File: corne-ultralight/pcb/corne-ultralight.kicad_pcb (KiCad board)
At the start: 2 copper layers, 275.5 x 105.6 mm, 132 parts, among them J2 OLED, J5 Breakaway_Tabs, J7 OLED, SW1 SW_PUSH, SW10 SW_PUSH, SW11 SW_PUSH, SW12 SW_PUSH, SW13 SW_PUSH, SW14 SW_PUSH, SW15 SW_PUSH, SW16 SW_PUSH, SW17 SW_PUSH, SW18 SW_PUSH, SW19 SW_PUSH, SW2 SW_PUSH, SW20 SW_PUSH, SW21 SW_PUSH, SW22 SW_PUSH, SW23 SW_PUSH, SW24 SW_PUSH, SW25 SW_PUSH, SW26 SW_PUSH, SW27 SW_PUSH, SW28 SW_PUSH, SW29 SW_PUSH, SW3 SW_PUSH, SW30 SW_PUSH, SW31 SW_PUSH, SW32 SW_PUSH, SW33 SW_PUSH, SW34 SW_PUSH, SW35 SW_PUSH, SW36 SW_PUSH, SW37 SW_PUSH, SW38 SW_PUSH, SW39 SW_PUSH, SW4 SW_PUSH, SW40 SW_PUSH, SW41 SW_PUSH, SW42 SW_PUSH, SW5 SW_PUSH, SW6 SW_PUSH, SW7 SW_PUSH, SW8 SW_PUSH, SW9 SW_PUSH, U1 ProMicro, U2 ProMicro

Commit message: PCB updated with additional components
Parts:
- added BATJ3: Conn_01x02_Female, Connector_JST:JST_PH_S2B-PH-K_1x02_P2.00mm_Horizontal, F.Cu at (129.4, 95.7)
- added BATJ4: Conn_01x02_Female, Connector_JST:JST_PH_S2B-PH-K_1x02_P2.00mm_Horizontal, F.Cu at (137.3, 95.7)
- added BATJ7: Conn_01x02_Female, Connector_JST:JST_PH_S2B-PH-K_1x02_P2.00mm_Horizontal, F.Cu at (183.7, 89.0)
- added BATJ8: Conn_01x02_Female, Connector_JST:JST_PH_S2B-PH-K_1x02_P2.00mm_Horizontal, F.Cu at (191.6, 89.0)
- added OL1: OLED, kbd:OLED_1side, F.Cu at (128.1, 104.7)
- added OL2: OLED, kbd:OLED_1side, F.Cu at (168.1, 106.5)
- BATJ1: footprint Connector_PinHeader_2.54mm:PinHeader_1x02_P2.54mm_Vertical -> Connector_JST:JST_PH_S2B-PH-K_1x02_P2.00mm_Horizontal
- BATJ5: renamed from BATJ3; footprint Connector_PinHeader_2.54mm:PinHeader_1x02_P2.54mm_Vertical -> Connector_JST:JST_PH_S2B-PH-K_1x02_P2.00mm_Horizontal
- D1, D10, D11, D12, D13, D14, D15, D16, D17, D18, D19, D2, D20, D21, D22, D23, D24, D25, D26, D27, D28, D29, D3, D30, D31, D32, D33, D34, D35, D36, D37, D38, D39, D4, D40, D41, D42, D5, D6, D7, D8, D9: footprint kbd:D3_TH_SMD_v2 -> kbd:D3_TH
- renumbered BATJ4 to BATJ6

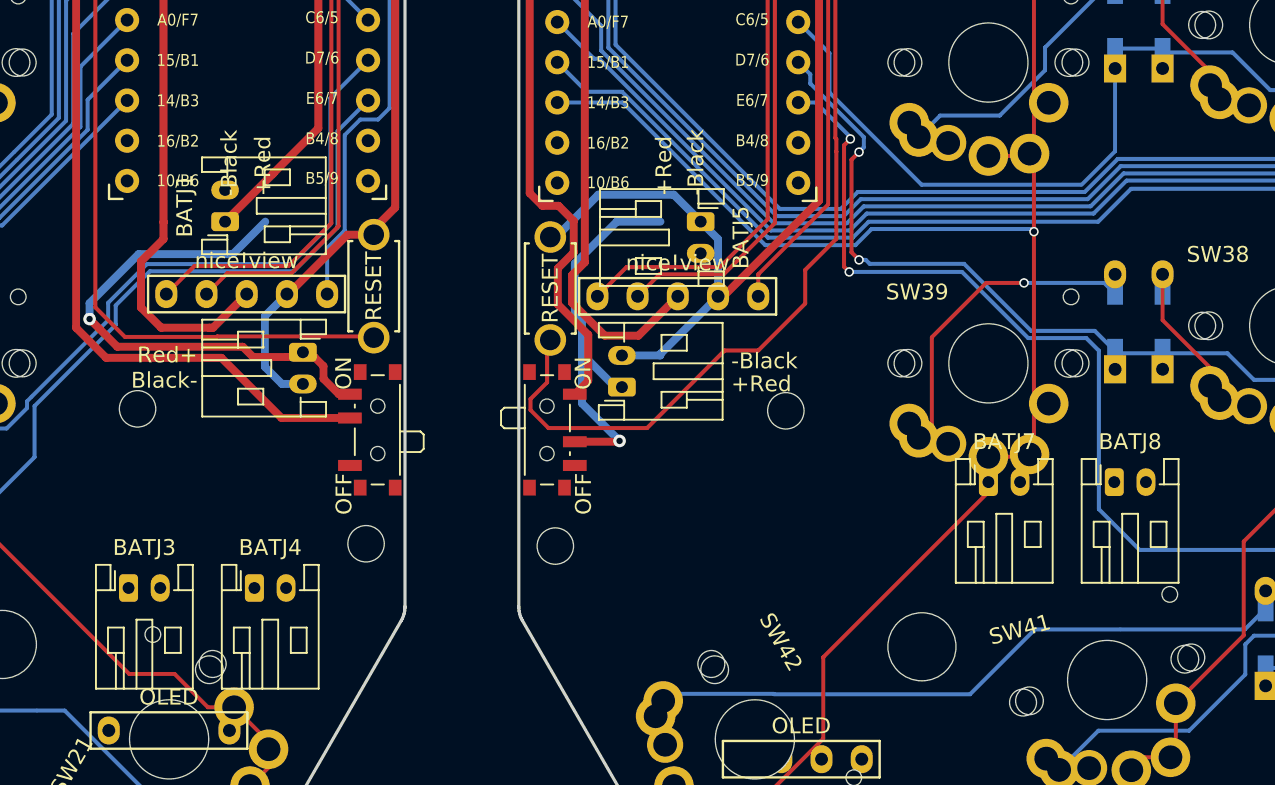
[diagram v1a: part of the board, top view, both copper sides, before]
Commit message: Bottom JST connectors aligned
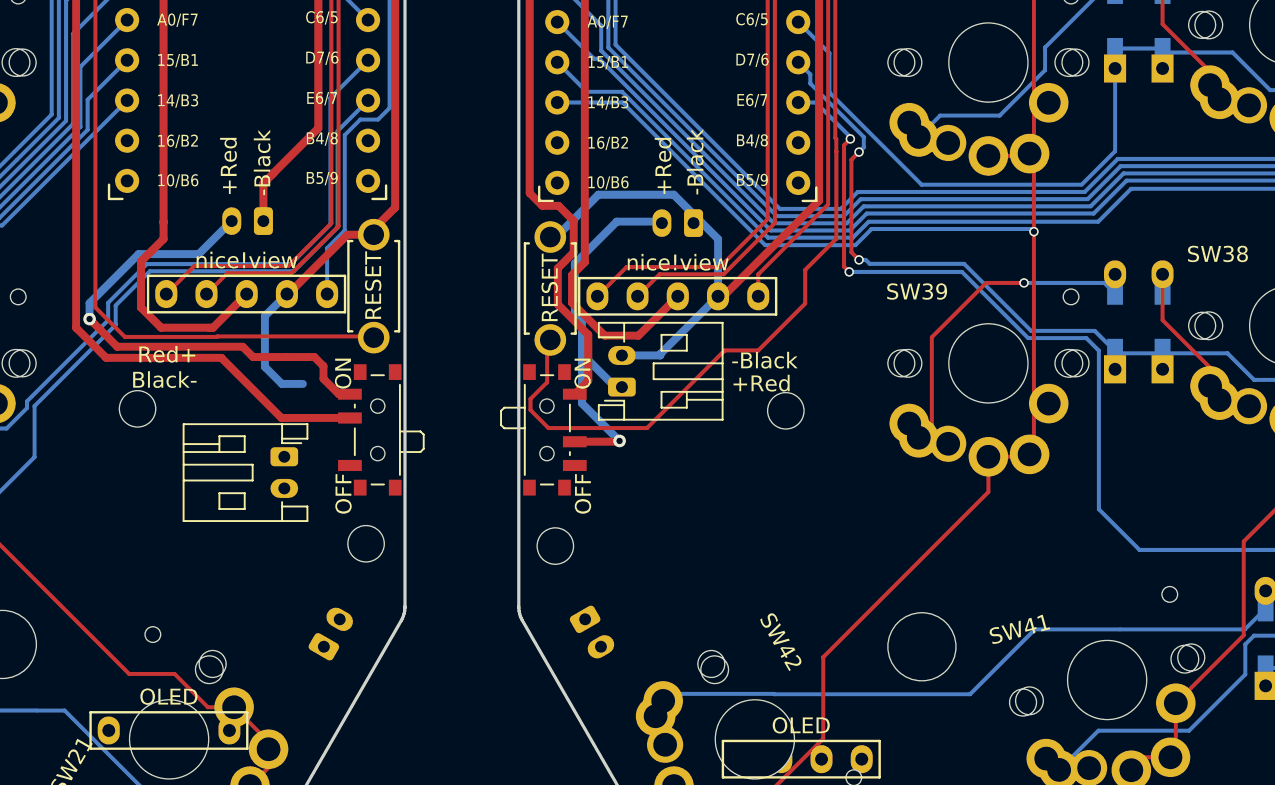
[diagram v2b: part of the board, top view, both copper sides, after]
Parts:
- removed the BATJ3 at (129.4, 95.7)
- removed BATJ8: Conn_01x02_Female, Connector_JST:JST_PH_S2B-PH-K_1x02_P2.00mm_Horizontal
- BATJ1: moved to B.Cu
- BATJ3: renamed from BATJ4; moved to B.Cu
- BATJ4: renamed from BATJ5; moved to B.Cu
- BATJ6: renamed from BATJ7; moved to B.Cu
- moved BATJ6 26.9 mm to (158.2, 97.7), turned to -60 degrees
- moved BATJ2 6.70 mm to (139.2, 87.4)
- moved BATJ3 5.75 mm to (141.7, 99.4), turned to 60 degrees
- moved BATJ1 2.42 mm to (137.9, 72.6), turned to 180 degrees
- moved BATJ4 0.46 mm to (165.1, 72.7), turned to 180 degrees
- renumbered BATJ6 to BATJ5
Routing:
- net Net-(BATJ1-Pin_2): track 33.1 -> 31.0 mm
- net GND: track 88.8 -> 87.7 mm

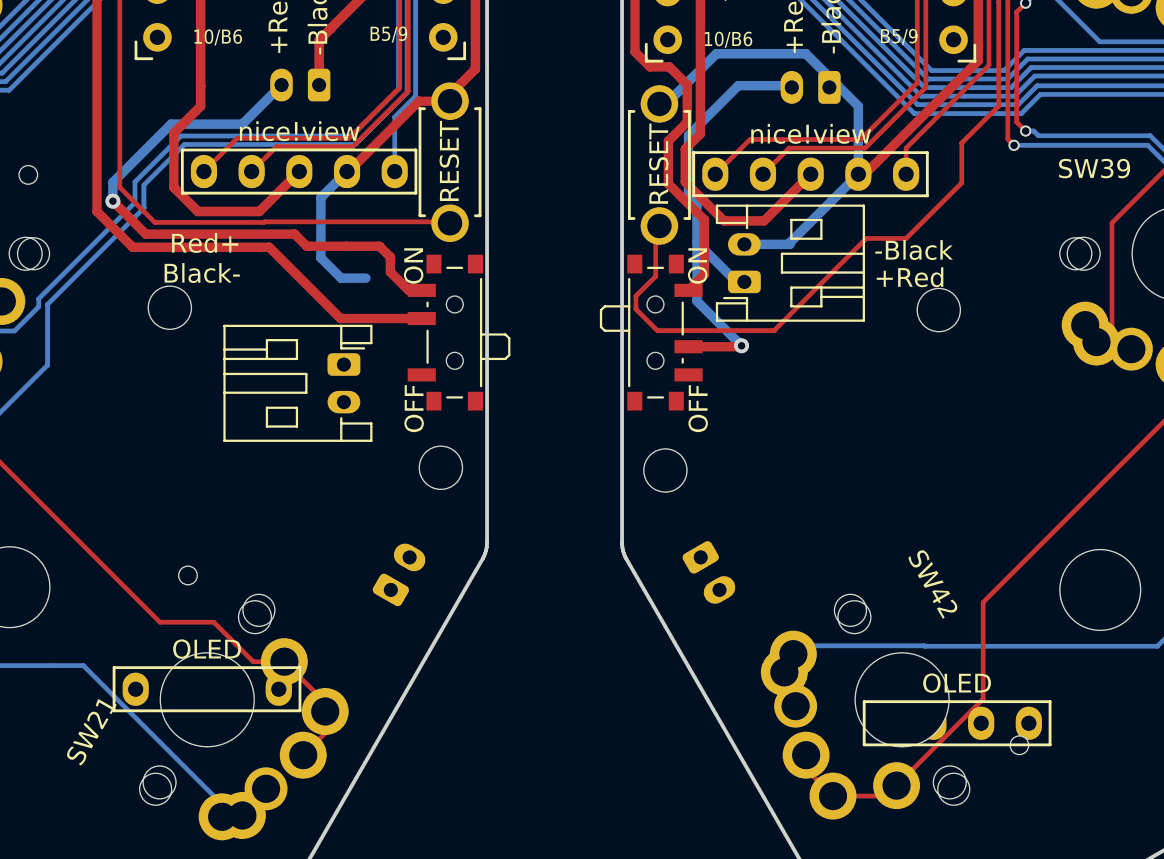
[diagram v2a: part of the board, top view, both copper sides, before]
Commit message: OLED aligned
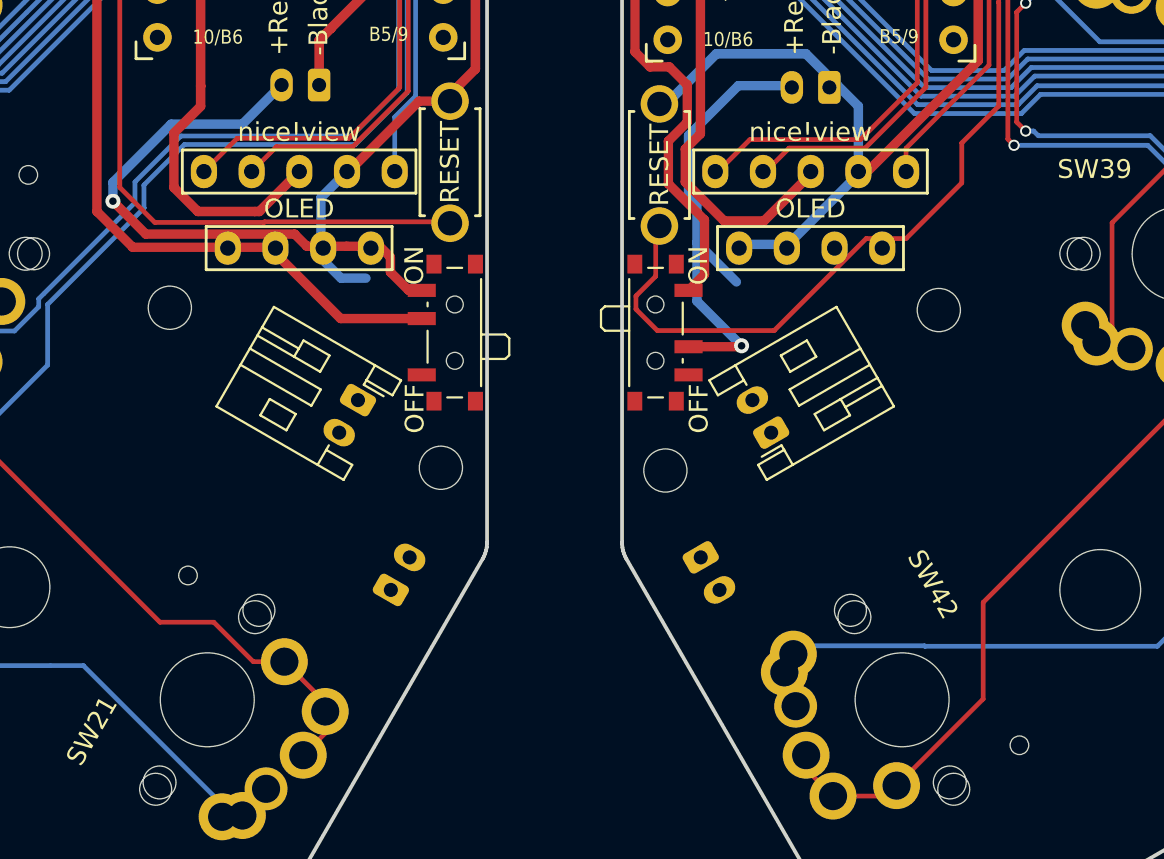
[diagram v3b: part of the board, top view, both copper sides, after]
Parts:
- moved OL2 26.5 mm to (160.3, 81.2)
- moved OL1 24.0 mm to (133.0, 81.2)
- moved BATJ5 8.15 mm to (162.0, 91.1), turned to 120 degrees
- moved BATJ2 2.04 mm to (140.0, 89.3), turned to -120 degrees
- moved J7 0.14 mm to (159.0, 77.2)

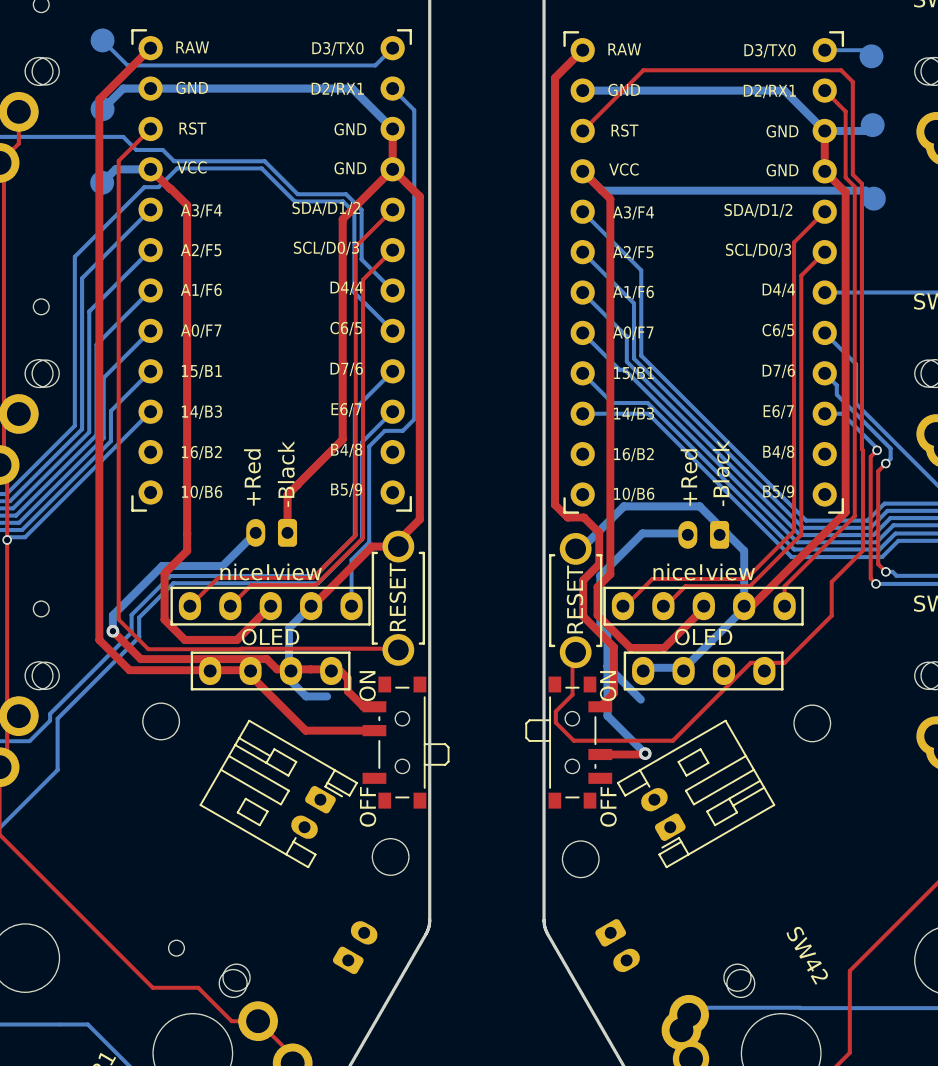
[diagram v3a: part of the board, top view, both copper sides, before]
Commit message: All JST connectors routed
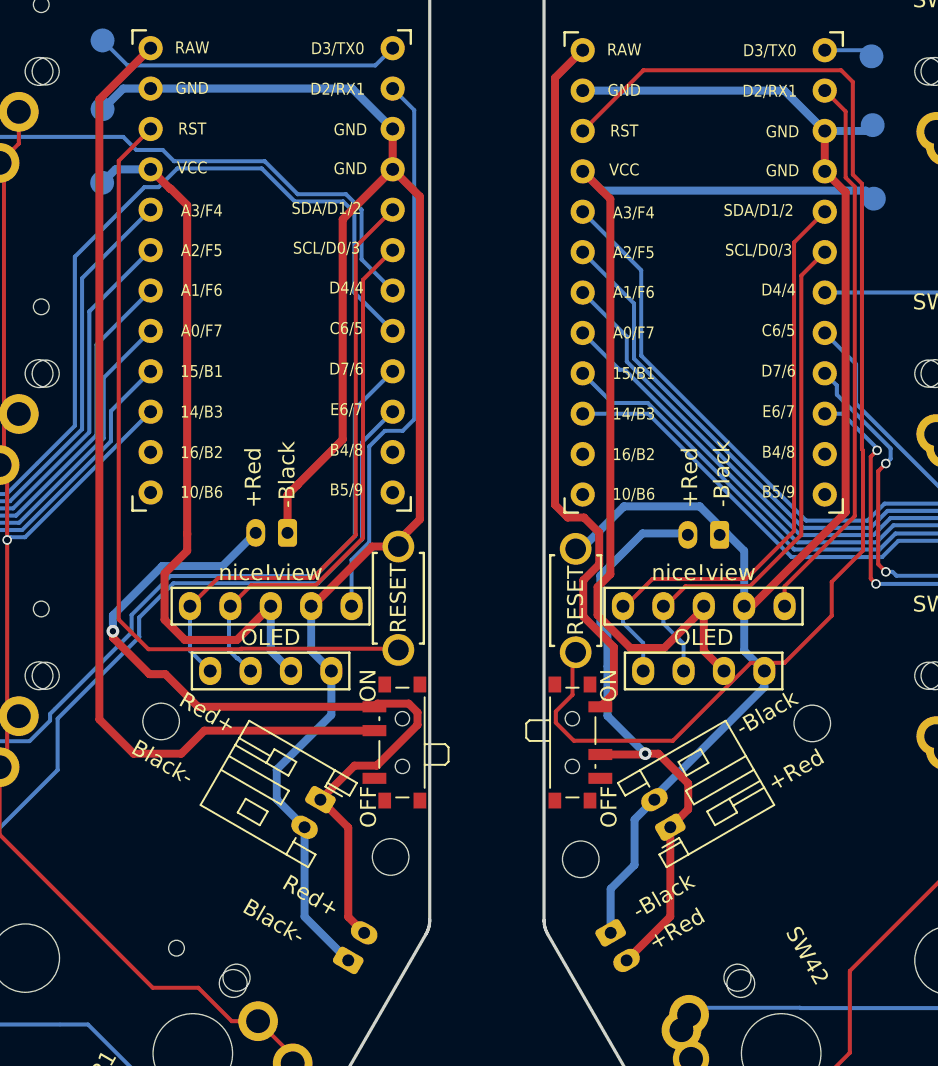
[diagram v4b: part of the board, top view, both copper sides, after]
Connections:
- OL1 pad 4: unconnected-(OL1-GND-Pad4) -> GND
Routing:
- net Net-(BATJ1-Pin_2): track 31.0 -> 52.1 mm
- net GND: track 87.7 -> 105.8 mm
- net GNDA: track 76.3 -> 93.8 mm
- net Net-(BATJ5-Pin_2): track 24.7 -> 37.9 mm
- net SCL: track 29.0 -> 34.1 mm
- net VDD: track 56.5 -> 61.3 mm
- net SCL_r: track 29.0 -> 33.6 mm
- net SDA: track 33.7 -> 38.3 mm
- net VCC: track 41.4 -> 46.0 mm
- net SDA_r: track 33.6 -> 38.2 mm
- net +BATT: track 58.2 -> 62.3 mm
